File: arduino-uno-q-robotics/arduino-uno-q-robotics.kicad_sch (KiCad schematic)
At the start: 4 parts, among them J1 Conn_02x30_Odd_Even, J2 Conn_02x30_Odd_Even, J3 Connector_FFC-FPC, J4 Connector_FFC-FPC

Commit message: Add Gyro/Accelerometer sensor
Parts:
- added R1, R2: 10k, symbol Device:R
- added R3: R, symbol Device:R
- added U1: LSM6DSO32, LGA-14L_2P5X3X0P83_STM, symbol robotics-symbols:LSM6DSO32
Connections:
- net +3.3V: now also R1.1, R2.1, R3.1, U1.5 (VDDIO), U1.8 (VDD)
- net GND: now also U1.6 (GND), U1.7 (GND)
- net MCU_I2C4_SCL: now also R1.2, U1.13 (SCL)
- net MCU_I2C4_SDA: now also R2.2, U1.14 (SDA)
- new net CS: R3.2, U1.12 (CS)
- no-connect marks 0 -> 5
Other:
- moved on the sheet: J3, J4

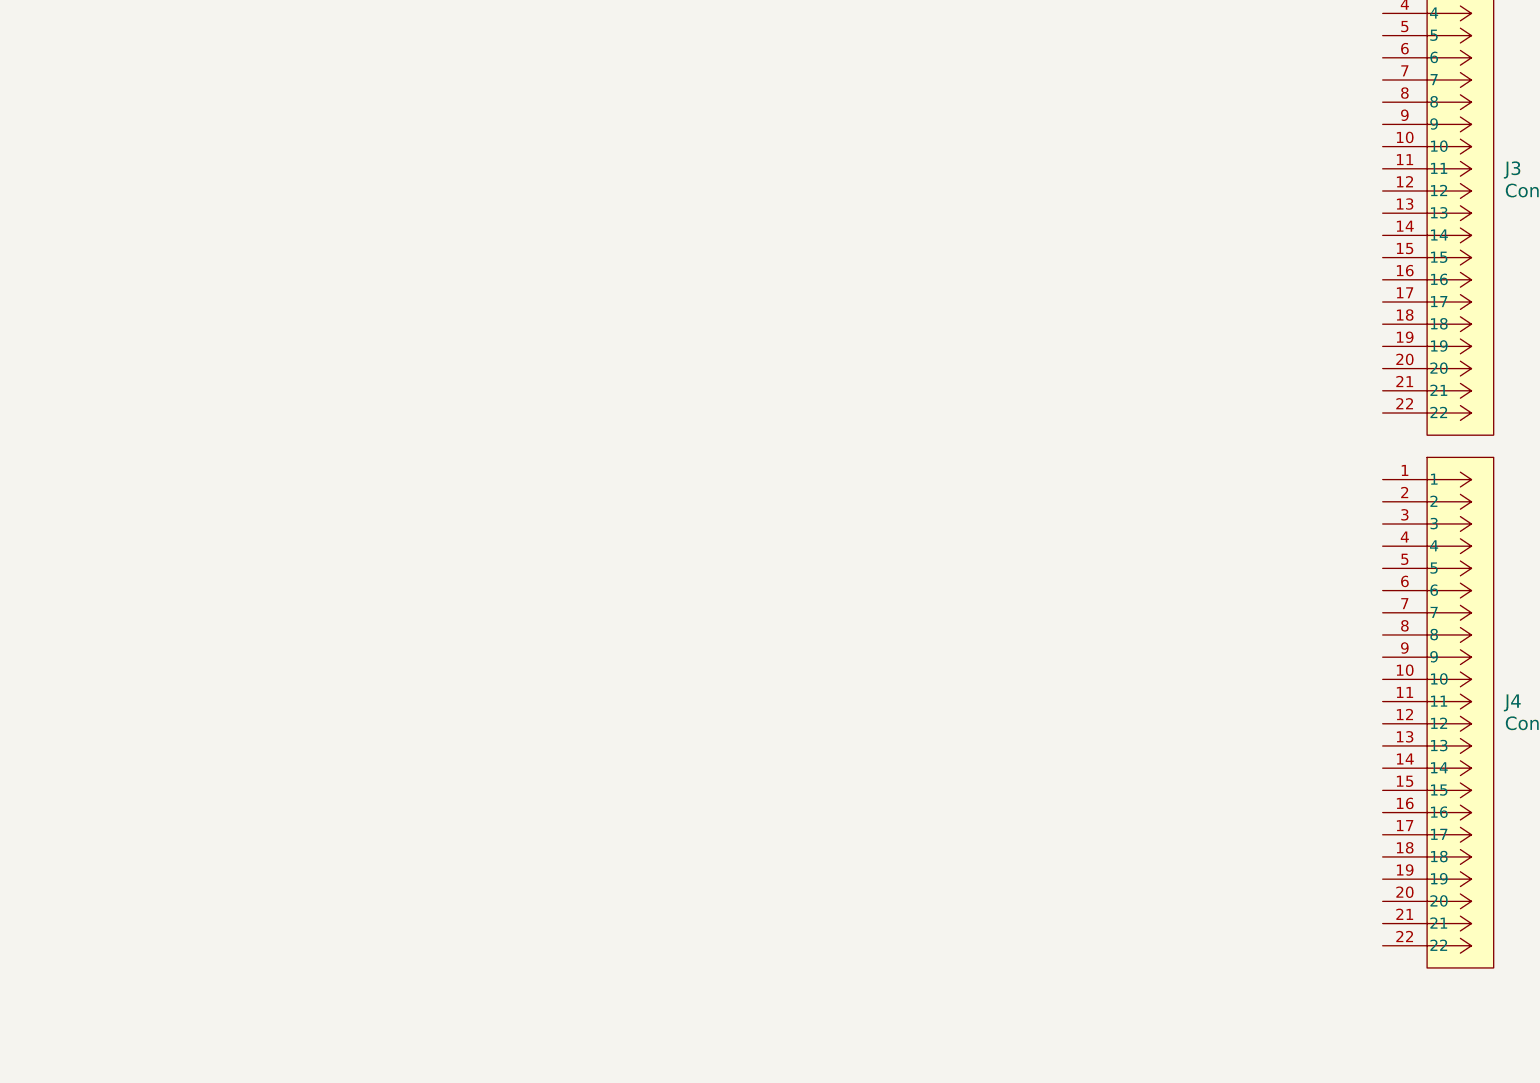
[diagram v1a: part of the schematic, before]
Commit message: Add I2C logic level shifter to schematic
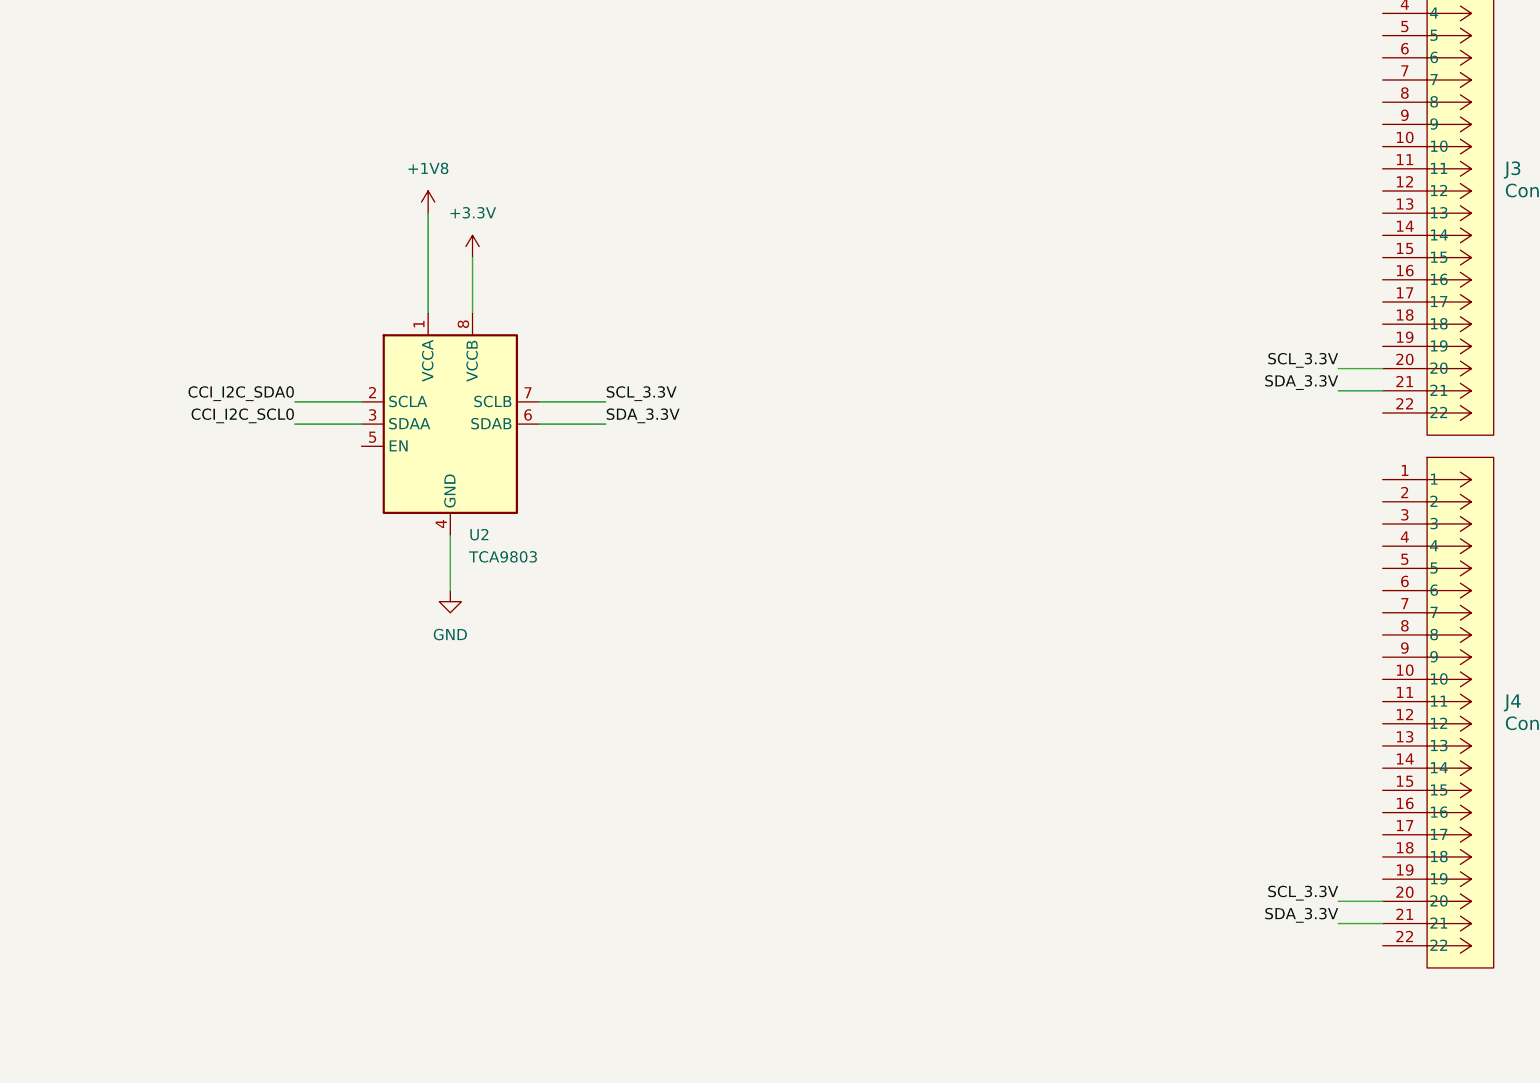
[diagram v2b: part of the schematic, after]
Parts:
- added U2: TCA9803, Package_SO:VSSOP-8_3x3mm_P0.65mm, symbol Interface:TCA9803
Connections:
- net +1V8: now also U2.1 (VCCA)
- net +3.3V: now also U2.8 (VCCB)
- net CCI_I2C_SCL0: now also U2.3 (SDAA)
- net CCI_I2C_SDA0: now also U2.2 (SCLA)
- net GND: now also U2.4 (GND)
- net SCL_3.3V: now reaches J3.20
- net SCL_3.3V: now also J4.20, U2.7 (SCLB)
- net SDA_3.3V: now reaches J3.21
- net SDA_3.3V: now also J4.21, U2.6 (SDAB)

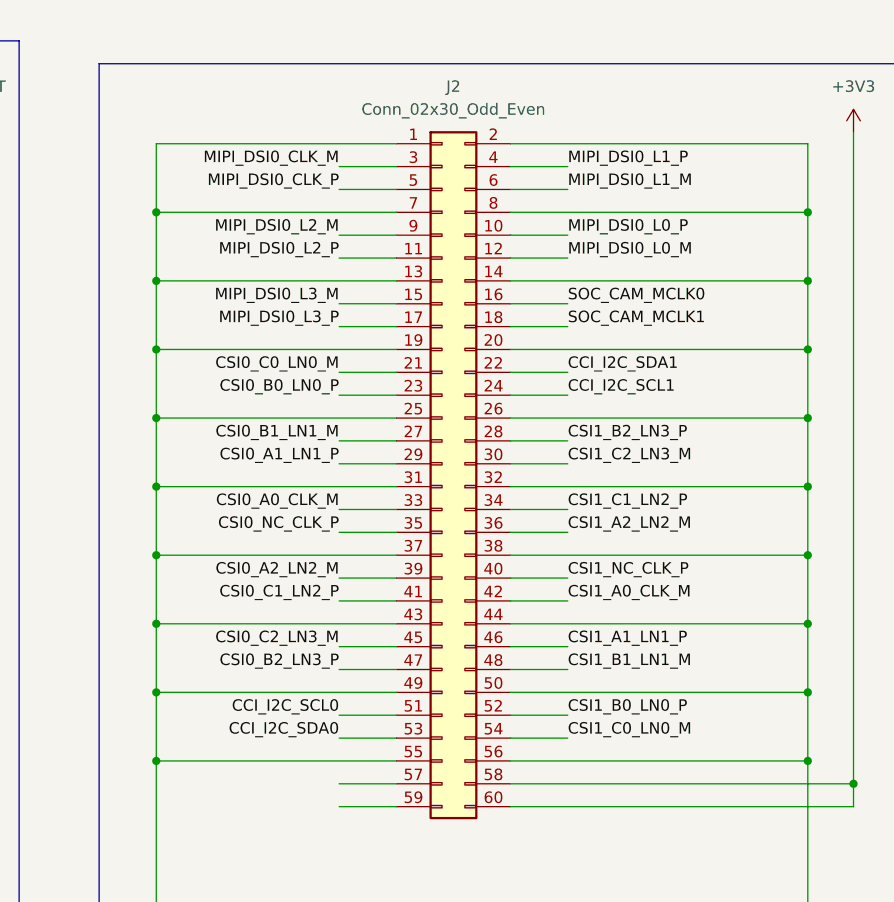
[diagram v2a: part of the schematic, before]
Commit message: Adjust JMEDIA labels for differential routing
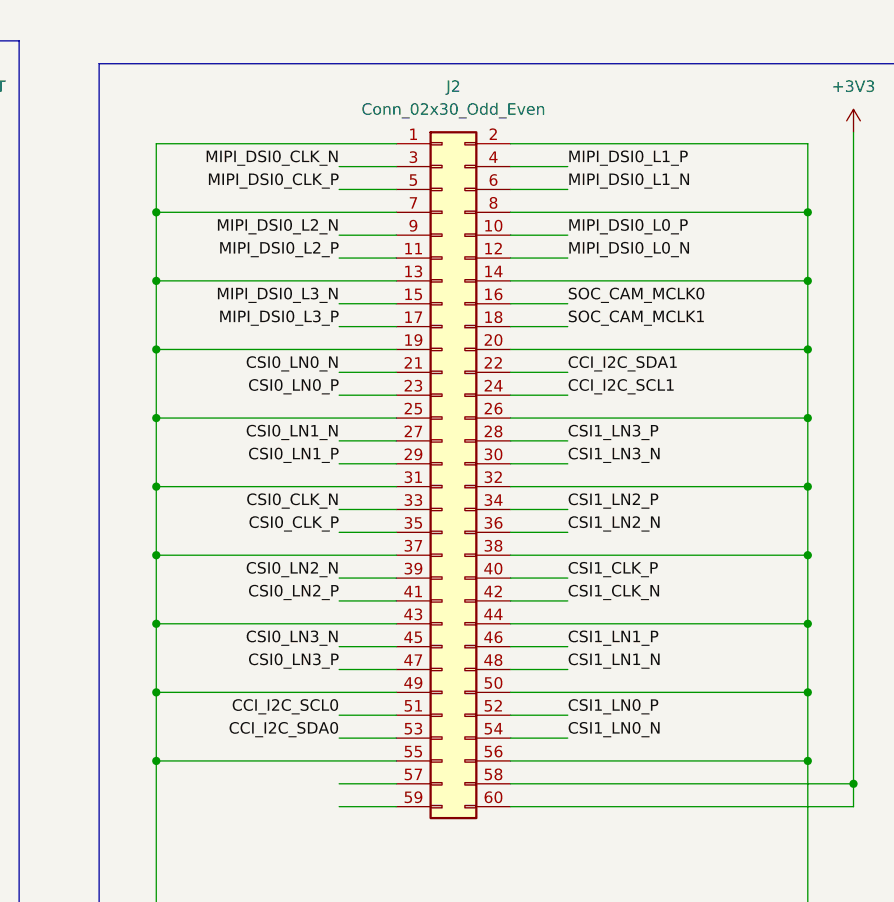
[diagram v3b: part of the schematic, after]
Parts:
- U1: footprint LGA-14L_2P5X3X0P83_STM -> robotics-footprints:LGA-14L_2P5X3X0P83_STM
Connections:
- net CSI0_A0_CLK_M renamed CSI0_CLK_N
- net CSI0_A1_LN1_P renamed CSI0_LN1_P
- net CSI0_A2_LN2_M renamed CSI0_LN2_N
- net CSI0_B0_LN0_P renamed CSI0_LN0_P
- net CSI0_B1_LN1_M renamed CSI0_LN1_N
- net CSI0_B2_LN3_P renamed CSI0_LN3_P
- net CSI0_C0_LN0_M renamed CSI0_LN0_N
- net CSI0_C1_LN2_P renamed CSI0_LN2_P
- net CSI0_C2_LN3_M renamed CSI0_LN3_N
- net CSI0_NC_CLK_P renamed CSI0_CLK_P
- net CSI1_A0_CLK_M renamed CSI1_CLK_N
- net CSI1_A1_LN1_P renamed CSI1_LN1_P
- net CSI1_A2_LN2_M renamed CSI1_LN2_N
- net CSI1_B0_LN0_P renamed CSI1_LN0_P
- net CSI1_B1_LN1_M renamed CSI1_LN1_N
- net CSI1_B2_LN3_P renamed CSI1_LN3_P
- net CSI1_C0_LN0_M renamed CSI1_LN0_N
- net CSI1_C1_LN2_P renamed CSI1_LN2_P
- net CSI1_C2_LN3_M renamed CSI1_LN3_N
- net CSI1_NC_CLK_P renamed CSI1_CLK_P
- net MIPI_DSI0_CLK_M renamed MIPI_DSI0_CLK_N
- net MIPI_DSI0_L0_M renamed MIPI_DSI0_L0_N
- net MIPI_DSI0_L1_M renamed MIPI_DSI0_L1_N
- net MIPI_DSI0_L2_M renamed MIPI_DSI0_L2_N
- net MIPI_DSI0_L3_M renamed MIPI_DSI0_L3_N
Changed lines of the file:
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@@
 		)
 	)
-	(label "MIPI_DSI0_L2_M"
+	(label "MIPI_DSI0_L2_N"
 		(at 146.05 41.91 180)
 		(effects
@@
 		)
 	)
-	(label "CSI0_C1_LN2_P"
+	(label "CSI0_LN2_P"
 		(at 146.05 82.55 180)
 		(effects
@@
 		)
 	)
-	(label "CSI0_B0_LN0_P"
+	(label "CSI0_LN0_P"
 		(at 146.05 59.69 180)
 		(effects
@@
 		)
 	)
-	(label "CSI0_A0_CLK_M"
+	(label "CSI0_CLK_N"
 		(at 146.05 72.39 180)
 		(effects
@@
 		)
 	)
-	(label "MIPI_DSI0_CLK_M"
+	(label "MIPI_DSI0_CLK_N"
 		(at 146.05 34.29 180)
 		(effects
@@
 		)
 	)
-	(label "CSI1_A0_CLK_M"
+	(label "CSI1_CLK_N"
 		(at 171.45 82.55 0)
 		(effects
@@
 		)
 	)
-	(label "CSI1_B2_LN3_P"
+	(label "CSI1_LN3_P"
 		(at 171.45 64.77 0)
 		(effects
@@
 		)
 	)
-	(label "CSI1_B1_LN1_M"
+	(label "CSI1_LN1_N"
 		(at 171.45 90.17 0)
 		(effects
@@
 		)
 	)
-	(label "CSI0_B2_LN3_P"
+	(label "CSI0_LN3_P"
 		(at 146.05 90.17 180)
 		(effects
@@
 		)
 	)
-	(label "CSI1_A1_LN1_P"
+	(label "CSI1_LN1_P"
 		(at 171.45 87.63 0)
 		(effects
@@
 		)
 	)
-	(label "CSI0_C2_LN3_M"
+	(label "CSI0_LN3_N"
 		(at 146.05 87.63 180)
 		(effects
@@
 		)
 	)
-	(label "CSI0_B1_LN1_M"
+	(label "CSI0_LN1_N"
 		(at 146.05 64.77 180)
 		(effects
@@
 		)
 	)
-	(label "CSI0_A2_LN2_M"
+	(label "CSI0_LN2_N"
 		(at 146.05 80.01 180)
 		(effects
@@
 		)
 	)
-	(label "CSI1_A2_LN2_M"
+	(label "CSI1_LN2_N"
 		(at 171.45 74.93 0)
 		(effects
@@
 		)
 	)
-	(label "CSI1_B0_LN0_P"
+	(label "CSI1_LN0_P"
 		(at 171.45 95.25 0)
 		(effects
@@
 		)
 	)
-	(label "CSI0_NC_CLK_P"
+	(label "CSI0_CLK_P"
 		(at 146.05 74.93 180)
 		(effects
@@
 		)
 	)
-	(label "CSI1_C1_LN2_P"
+	(label "CSI1_LN2_P"
 		(at 171.45 72.39 0)
 		(effects
@@
 		)
 	)
-	(label "CSI1_C2_LN3_M"
+	(label "CSI1_LN3_N"
 		(at 171.45 67.31 0)
 		(effects
@@
 		)
 	)
-	(label "MIPI_DSI0_L0_M"
+	(label "MIPI_DSI0_L0_N"
 		(at 171.45 44.45 0)
 		(effects
@@
 		)
 	)
-	(label "MIPI_DSI0_L1_M"
+	(label "MIPI_DSI0_L1_N"
 		(at 171.45 36.83 0)
 		(effects
@@
 		)
 	)
-	(label "MIPI_DSI0_L3_M"
+	(label "MIPI_DSI0_L3_N"
 		(at 146.05 49.53 180)
 		(effects
@@
 		)
 	)
-	(label "CSI0_A1_LN1_P"
+	(label "CSI0_LN1_P"
 		(at 146.05 67.31 180)
 		(effects
@@
 		)
 	)
-	(label "CSI0_C0_LN0_M"
+	(label "CSI0_LN0_N"
 		(at 146.05 57.15 180)
 		(effects
@@
 		)
 	)
-	(label "CSI1_C0_LN0_M"
+	(label "CSI1_LN0_N"
 		(at 171.45 97.79 0)
 		(effects
@@
 		)
 	)
-	(label "CSI1_NC_CLK_P"
+	(label "CSI1_CLK_P"
 		(at 171.45 80.01 0)
 		(effects
@@
 			)
 		)
-		(property "Footprint" "LGA-14L_2P5X3X0P83_STM"
+		(property "Footprint" "robotics-footprints:LGA-14L_2P5X3X0P83_STM"
 			(at 56.642 268.224 0)
 			(effects
